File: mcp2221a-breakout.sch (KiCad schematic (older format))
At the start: 25 parts, among them J1 USB_B_Micro, J2 LEFT, J3 RIGHT, U1 MCP1700-3302E, U2 MCP2221AxSL

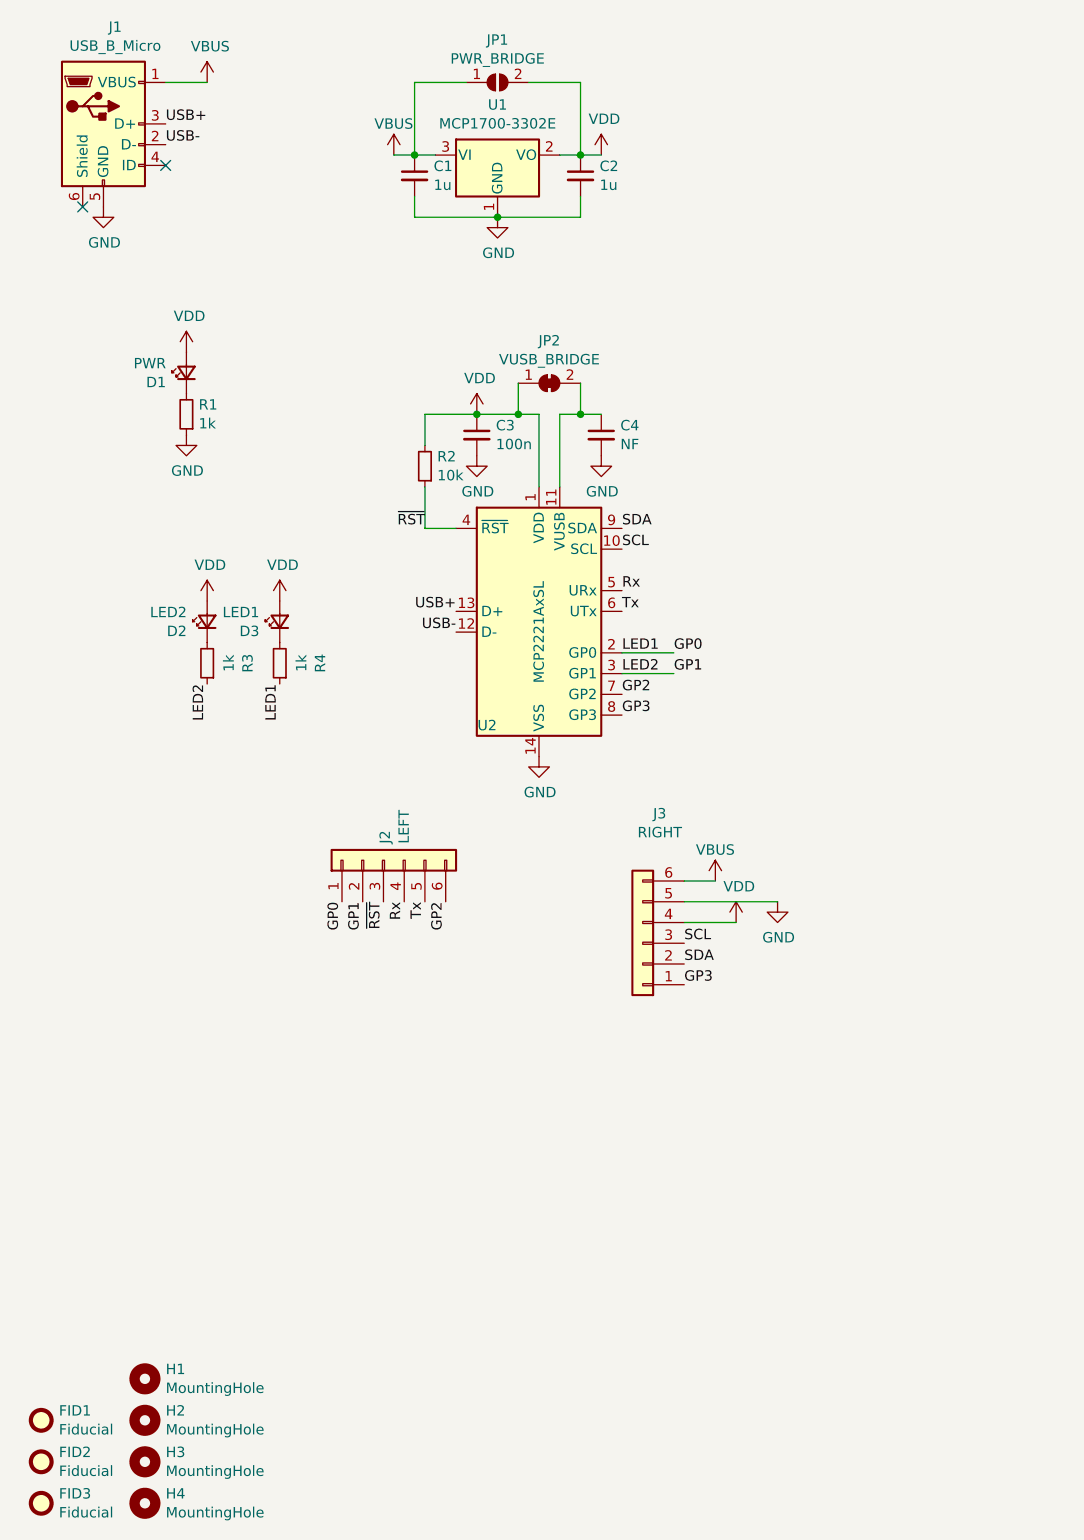
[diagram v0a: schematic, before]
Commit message: Various Tweaks
* Tidied up the schematic
* Added I2C pullup resistors
* Changed labels on LED1 & LED2 to Rx & Tx
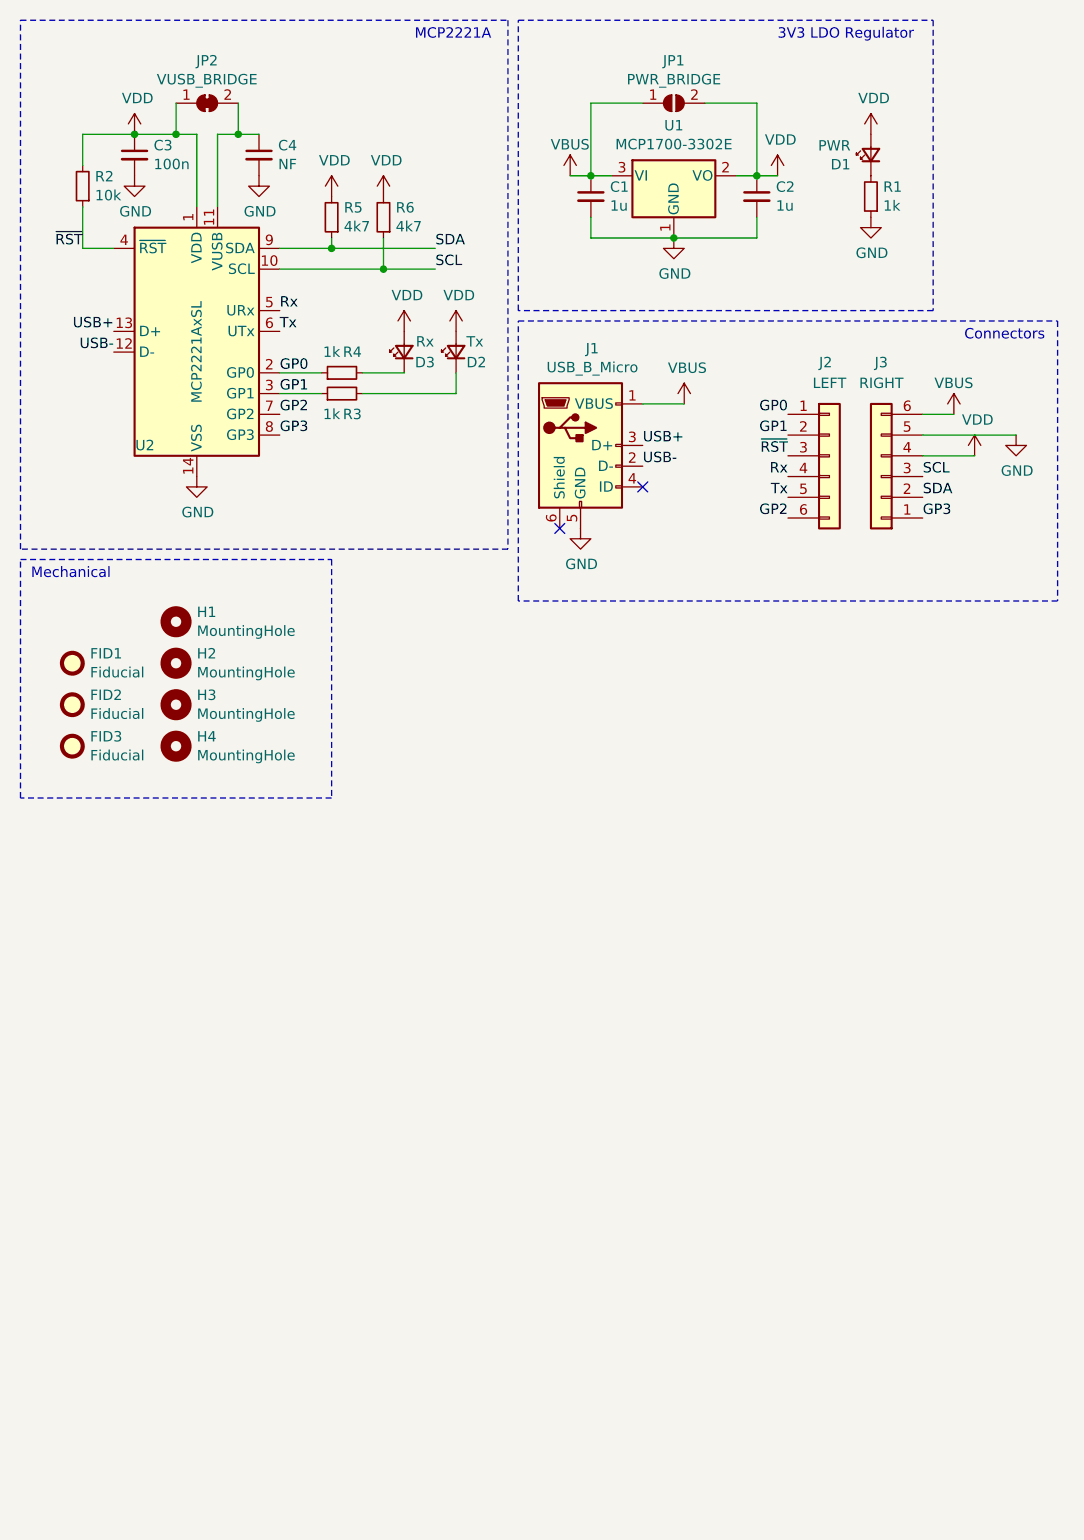
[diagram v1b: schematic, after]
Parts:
- added R5, R6: 4k7, Resistor_SMD:R_0603_1608Metric, symbol Device:R_Small
- D2: value LED2 -> Tx
- D3: value LED1 -> Rx
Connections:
- net SCL: now also R6.1
- net SDA: now also R5.1
- net VDD: now also R5.2, R6.2
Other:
- note added: "3V3 LDO Regulator\n"
- note added: "Connectors\n"
- note added: "MCP2221A"
- note added: "Mechanical"
- moved on the sheet: C1, C2, C3, C4, D1, D2, D3, FID1, FID2, FID3, H1, H2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
